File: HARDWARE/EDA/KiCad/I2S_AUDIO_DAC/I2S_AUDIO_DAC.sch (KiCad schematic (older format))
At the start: 28 parts, among them J1 Conn_01x07_Male, J2 Conn_01x010_Male, U1 L78L33_TO92, U2 UDA1334ATS

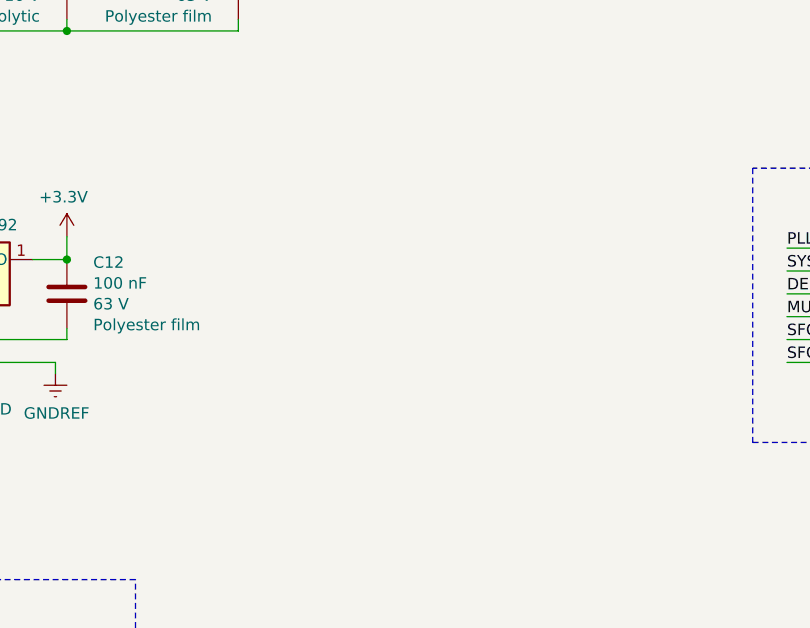
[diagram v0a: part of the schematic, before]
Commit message: add led to schematic and adjust pcb
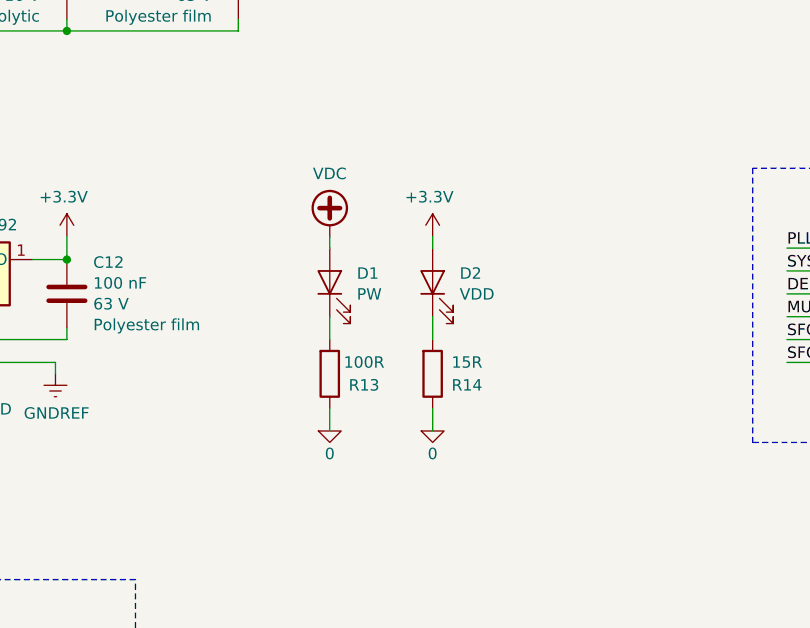
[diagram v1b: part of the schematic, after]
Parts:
- added D1: PW, LED_THT:LED_D5.0mm, symbol Device:LED
- added D2: VDD, LED_THT:LED_D5.0mm, symbol Device:LED
- added R13: 100R, Resistor_THT:R_Axial_DIN0207_L6.3mm_D2.5mm_P7.62mm_Horizontal, symbol Device:R
- added R14: 15R, Resistor_THT:R_Axial_DIN0207_L6.3mm_D2.5mm_P7.62mm_Horizontal, symbol Device:R
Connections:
- net +3V3: now also D2.2 (A)
- net 0: now also R13.1, R14.1
- net VDC: now also D1.2 (A)
- new net: D1.1 (K), R13.2
- new net: D2.1 (K), R14.2
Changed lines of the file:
@@
 Wire Wire Line
 	2100 4700 2100 4800
+$Comp
+L Device:LED D1
+U 1 1 61B490AE
+P 3700 4450
+F 0 "D1" V 3739 4332 50  0000 R CNN
+F 1 "PW" V 3648 4332 50  0000 R CNN
+F 2 "LED_THT:LED_D5.0mm" H 3700 4450 50  0001 C CNN
+F 3 "~" H 3700 4450 50  0001 C CNN
+	1    3700 4450
+	0    -1   -1   0
+$EndComp
+Wire Wire Line
+	3700 4700 3700 4600
+$Comp
+L pspice:0 #GND0103
+U 1 1 61B5C6ED
+P 3700 5100
+F 0 "#GND0103" H 3700 5000 50  0001 C CNN
+F 1 "0" H 3700 5000 50  0000 C CNN
+F 2 "" H 3700 5100 50  0001 C CNN
+F 3 "~" H 3700 5100 50  0001 C CNN
+	1    3700 5100
+	1    0    0    -1
+$EndComp
+Wire Wire Line
+	3700 5100 3700 5000
+$Comp
+L power:VDC #PWR0123
+U 1 1 61B9C1D4
+P 3700 4250
+F 0 "#PWR0123" H 3700 4150 50  0001 C CNN
+F 1 "VDC" H 3700 4525 50  0000 C CNN
+F 2 "" H 3700 4250 50  0001 C CNN
+F 3 "" H 3700 4250 50  0001 C CNN
+	1    3700 4250
+	1    0    0    -1
+$EndComp
+Wire Wire Line
+	3700 4250 3700 4300
+$Comp
+L Device:LED D2
+U 1 1 61BA2E5F
+P 4150 4450
+F 0 "D2" V 4189 4332 50  0000 R CNN
+F 1 "VDD" V 4098 4332 50  0000 R CNN
+F 2 "LED_THT:LED_D5.0mm" H 4150 4450 50  0001 C CNN
+F 3 "~" H 4150 4450 50  0001 C CNN
+	1    4150 4450
+	0    -1   -1   0
+$EndComp
+$Comp
+L Device:R R14
+U 1 1 61BA2E65
+P 4150 4850
+F 0 "R14" H 4300 4900 50  0000 C CNN
+F 1 "15R" H 4300 4800 50  0000 C CNN
+F 2 "Resistor_THT:R_Axial_DIN0207_L6.3mm_D2.5mm_P7.62mm_Horizontal" V 4080 4850 50  0001 C CNN
+F 3 "~" H 4150 4850 50  0001 C CNN
+	1    4150 4850
+	1    0    0    1
+$EndComp
+Wire Wire Line
+	4150 4700 4150 4600
+$Comp
+L pspice:0 #GND0104
+U 1 1 61BA2E6C
+P 4150 5100
+F 0 "#GND0104" H 4150 5000 50  0001 C CNN
+F 1 "0" H 4150 5000 50  0000 C CNN
+F 2 "" H 4150 5100 50  0001 C CNN
+F 3 "~" H 4150 5100 50  0001 C CNN
+	1    4150 5100
+	1    0    0    -1
+$EndComp
+Wire Wire Line
+	4150 5100 4150 5000
+Wire Wire Line
+	4150 4250 4150 4300
+$Comp
+L power:+3.3V #PWR0124
+U 1 1 61BBA3E0
+P 4150 4250
+F 0 "#PWR0124" H 4150 4100 50  0001 C CNN
+F 1 "+3.3V" H 4165 4423 50  0000 C CNN
+F 2 "" H 4150 4250 50  0001 C CNN
+F 3 "" H 4150 4250 50  0001 C CNN
+	1    4150 4250
+	-1   0    0    -1
+$EndComp
+$Comp
+L Device:R R13
+U 1 1 61B5047D
+P 3700 4850
+F 0 "R13" H 3850 4900 50  0000 C CNN
+F 1 "100R" H 3850 4800 50  0000 C CNN
+F 2 "Resistor_THT:R_Axial_DIN0207_L6.3mm_D2.5mm_P7.62mm_Horizontal" V 3630 4850 50  0001 C CNN
+F 3 "~" H 3700 4850 50  0001 C CNN
+	1    3700 4850
+	1    0    0    1
+$EndComp
 $EndSCHEMATC

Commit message: pcb finished
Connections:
- net +3V3: now also R14.2; no longer D2.2 (A)
- net 0: now also D1.1 (K), D2.1 (K); no longer R13.1, R14.1
- net VDC: now also R13.2; no longer D1.2 (A)
- new net: D1.2 (A), R13.1
- new net: D2.2 (A), R14.1
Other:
- moved on the sheet: D1, D2, R13, R14
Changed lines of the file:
@@
 	2100 4700 2100 4800
-$Comp
-L Device:LED D1
-U 1 1 61B490AE
-P 3700 4450
-F 0 "D1" V 3739 4332 50  0000 R CNN
-F 1 "PW" V 3648 4332 50  0000 R CNN
-F 2 "LED_THT:LED_D5.0mm" H 3700 4450 50  0001 C CNN
-F 3 "~" H 3700 4450 50  0001 C CNN
-	1    3700 4450
-	0    -1   -1   0
-$EndComp
-Wire Wire Line
-	3700 4700 3700 4600
 $Comp
 L pspice:0 #GND0103
@@
 	1    0    0    -1
 $EndComp
-Wire Wire Line
-	3700 4250 3700 4300
-$Comp
-L Device:LED D2
-U 1 1 61BA2E5F
-P 4150 4450
-F 0 "D2" V 4189 4332 50  0000 R CNN
-F 1 "VDD" V 4098 4332 50  0000 R CNN
-F 2 "LED_THT:LED_D5.0mm" H 4150 4450 50  0001 C CNN
-F 3 "~" H 4150 4450 50  0001 C CNN
-	1    4150 4450
-	0    -1   -1   0
-$EndComp
 $Comp
 L Device:R R14
 U 1 1 61BA2E65
-P 4150 4850
-F 0 "R14" H 4300 4900 50  0000 C CNN
-F 1 "15R" H 4300 4800 50  0000 C CNN
-F 2 "Resistor_THT:R_Axial_DIN0207_L6.3mm_D2.5mm_P7.62mm_Horizontal" V 4080 4850 50  0001 C CNN
-F 3 "~" H 4150 4850 50  0001 C CNN
-	1    4150 4850
+P 4150 4450
+F 0 "R14" H 4300 4500 50  0000 C CNN
+F 1 "15R" H 4300 4400 50  0000 C CNN
+F 2 "Resistor_THT:R_Axial_DIN0207_L6.3mm_D2.5mm_P7.62mm_Horizontal" V 4080 4450 50  0001 C CNN
+F 3 "~" H 4150 4450 50  0001 C CNN
+	1    4150 4450
 	1    0    0    1
 $EndComp
-Wire Wire Line
-	4150 4700 4150 4600
 $Comp
 L pspice:0 #GND0104
@@
 Wire Wire Line
 	4150 5100 4150 5000
-Wire Wire Line
-	4150 4250 4150 4300
 $Comp
 L power:+3.3V #PWR0124
@@
 L Device:R R13
 U 1 1 61B5047D
+P 3700 4450
+F 0 "R13" H 3850 4500 50  0000 C CNN
+F 1 "100R" H 3850 4400 50  0000 C CNN
+F 2 "Resistor_THT:R_Axial_DIN0207_L6.3mm_D2.5mm_P7.62mm_Horizontal" V 3630 4450 50  0001 C CNN
+F 3 "~" H 3700 4450 50  0001 C CNN
+	1    3700 4450
+	1    0    0    1
+$EndComp
+Wire Wire Line
+	4150 4250 4150 4300
+Wire Wire Line
+	4150 4700 4150 4600
+$Comp
+L Device:LED D2
+U 1 1 61BA2E5F
+P 4150 4850
+F 0 "D2" V 4189 4732 50  0000 R CNN
+F 1 "VDD" V 4098 4732 50  0000 R CNN
+F 2 "LED_THT:LED_D5.0mm" H 4150 4850 50  0001 C CNN
+F 3 "~" H 4150 4850 50  0001 C CNN
+	1    4150 4850
+	0    -1   -1   0
+$EndComp
+Wire Wire Line
+	3700 4250 3700 4300
+Wire Wire Line
+	3700 4700 3700 4600
+$Comp
+L Device:LED D1
+U 1 1 61B490AE
 P 3700 4850
-F 0 "R13" H 3850 4900 50  0000 C CNN
-F 1 "100R" H 3850 4800 50  0000 C CNN
-F 2 "Resistor_THT:R_Axial_DIN0207_L6.3mm_D2.5mm_P7.62mm_Horizontal" V 3630 4850 50  0001 C CNN
+F 0 "D1" V 3739 4732 50  0000 R CNN
+F 1 "PW" V 3648 4732 50  0000 R CNN
+F 2 "LED_THT:LED_D5.0mm" H 3700 4850 50  0001 C CNN
 F 3 "~" H 3700 4850 50  0001 C CNN
 	1    3700 4850
-	1    0    0    1
+	0    -1   -1   0
 $EndComp
 $EndSCHEMATC
